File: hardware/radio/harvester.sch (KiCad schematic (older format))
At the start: 31 parts, among them U201 LTC3331

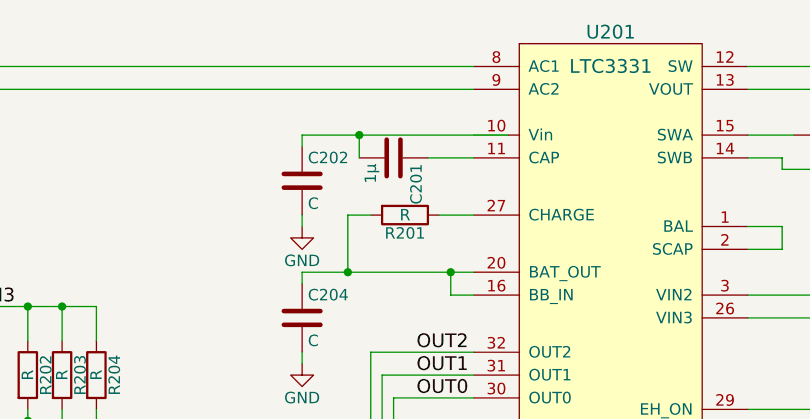
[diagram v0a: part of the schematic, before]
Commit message: Add accelerometer to schematic
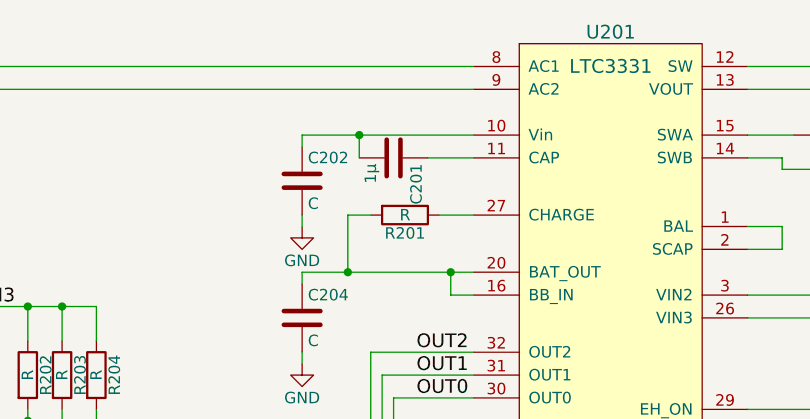
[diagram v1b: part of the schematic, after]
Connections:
- net at U201.10 (Vin): now also C201.2, C202.1
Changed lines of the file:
@@
 LIBS:sensors
 LIBS:rfcom
+LIBS:radio-cache
 EELAYER 25 0
 EELAYER END
@@
 $EndComp
 $Comp
-L GND #PWR014
+L GND #PWR202
 U 1 1 55E9B04F
 P 4050 2900
-F 0 "#PWR014" H 4050 2650 50  0001 C CNN
+F 0 "#PWR202" H 4050 2650 50  0001 C CNN
 F 1 "GND" H 4050 2750 50  0000 C CNN
 F 2 "" H 4050 2900 60  0000 C CNN
@@
 $EndComp
 $Comp
-L GND #PWR015
+L GND #PWR204
 U 1 1 55E9B130
 P 4050 3500
-F 0 "#PWR015" H 4050 3250 50  0001 C CNN
+F 0 "#PWR204" H 4050 3250 50  0001 C CNN
 F 1 "GND" H 4050 3350 50  0000 C CNN
 F 2 "" H 4050 3500 60  0000 C CNN
@@
 Connection ~ 2350 2850
 Wire Wire Line
-	4050 2500 4950 2500
-Wire Wire Line
 	4800 2600 4600 2600
 Wire Wire Line
@@
 Connection ~ 3000 3250
 $Comp
-L GND #PWR016
+L GND #PWR207
 U 1 1 55E9B68B
 P 2850 4450
-F 0 "#PWR016" H 2850 4200 50  0001 C CNN
+F 0 "#PWR207" H 2850 4200 50  0001 C CNN
 F 1 "GND" H 2850 4300 50  0000 C CNN
 F 2 "" H 2850 4450 60  0000 C CNN
@@
 Connection ~ 3000 6350
 $Comp
-L GND #PWR017
+L GND #PWR212
 U 1 1 55E9C430
 P 2850 7500
-F 0 "#PWR017" H 2850 7250 50  0001 C CNN
+F 0 "#PWR212" H 2850 7250 50  0001 C CNN
 F 1 "GND" H 2850 7350 50  0000 C CNN
 F 2 "" H 2850 7500 60  0000 C CNN
@@
 	4800 5300 4800 5950
 $Comp
-L GND #PWR018
+L GND #PWR210
 U 1 1 55E9C656
 P 4800 5950
-F 0 "#PWR018" H 4800 5700 50  0001 C CNN
+F 0 "#PWR210" H 4800 5700 50  0001 C CNN
 F 1 "GND" H 4800 5800 50  0000 C CNN
 F 2 "" H 4800 5950 60  0000 C CNN
@@
 Connection ~ 3000 4800
 $Comp
-L GND #PWR019
+L GND #PWR211
 U 1 1 55E9DB9C
 P 2850 6100
-F 0 "#PWR019" H 2850 5850 50  0001 C CNN
+F 0 "#PWR211" H 2850 5850 50  0001 C CNN
 F 1 "GND" H 2850 5950 50  0000 C CNN
 F 2 "" H 2850 6100 60  0000 C CNN
@@
 	5400 5600 5400 5700
 $Comp
-L GND #PWR020
+L GND #PWR208
 U 1 1 55E9FF2E
 P 5400 5700
-F 0 "#PWR020" H 5400 5450 50  0001 C CNN
+F 0 "#PWR208" H 5400 5450 50  0001 C CNN
 F 1 "GND" H 5400 5550 50  0000 C CNN
 F 2 "" H 5400 5700 60  0000 C CNN
@@
 	7700 2850 7700 3000
 $Comp
-L GND #PWR021
+L GND #PWR203
 U 1 1 55EA0A97
 P 7700 3000
-F 0 "#PWR021" H 7700 2750 50  0001 C CNN
+F 0 "#PWR203" H 7700 2750 50  0001 C CNN
 F 1 "GND" H 7700 2850 50  0000 C CNN
 F 2 "" H 7700 3000 60  0000 C CNN
@@
 	6700 4150 6700 4250
 $Comp
-L GND #PWR022
+L GND #PWR206
 U 1 1 55EA354D
 P 6700 4250
-F 0 "#PWR022" H 6700 4000 50  0001 C CNN
+F 0 "#PWR206" H 6700 4000 50  0001 C CNN
 F 1 "GND" H 6700 4100 50  0000 C CNN
 F 2 "" H 6700 4250 60  0000 C CNN
@@
 $EndComp
 $Comp
-L GND #PWR023
+L GND #PWR205
 U 1 1 55EA359B
 P 6300 4250
-F 0 "#PWR023" H 6300 4000 50  0001 C CNN
+F 0 "#PWR205" H 6300 4000 50  0001 C CNN
 F 1 "GND" H 6300 4100 50  0000 C CNN
 F 2 "" H 6300 4250 60  0000 C CNN
@@
 Connection ~ 4400 5850
 $Comp
-L GND #PWR024
+L GND #PWR209
 U 1 1 55EA7D40
 P 4400 5950
-F 0 "#PWR024" H 4400 5700 50  0001 C CNN
+F 0 "#PWR209" H 4400 5700 50  0001 C CNN
 F 1 "GND" H 4400 5800 50  0000 C CNN
 F 2 "" H 4400 5950 60  0000 C CNN
@@
 $EndComp
 $Comp
-L GND #PWR025
+L GND #PWR201
 U 1 1 55EB3C4E
 P 8300 2700
-F 0 "#PWR025" H 8300 2450 50  0001 C CNN
+F 0 "#PWR201" H 8300 2450 50  0001 C CNN
 F 1 "GND" H 8300 2550 50  0000 C CNN
 F 2 "" H 8300 2700 60  0000 C CNN
@@
 Text HLabel 8400 2500 2    60   Output ~ 0
 GND
+Wire Wire Line
+	4050 2500 4800 2500
 $EndSCHEMATC
